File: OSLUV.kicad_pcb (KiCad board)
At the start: 4 copper layers, 110 x 50 mm, 72 parts, among them IC1 NCP12510ASN65T1G, IC2 SFH6156-3, Q1 STD3NK80ZT4, Q2 BAT847B, T1 750343466, U2 TL432DBZ

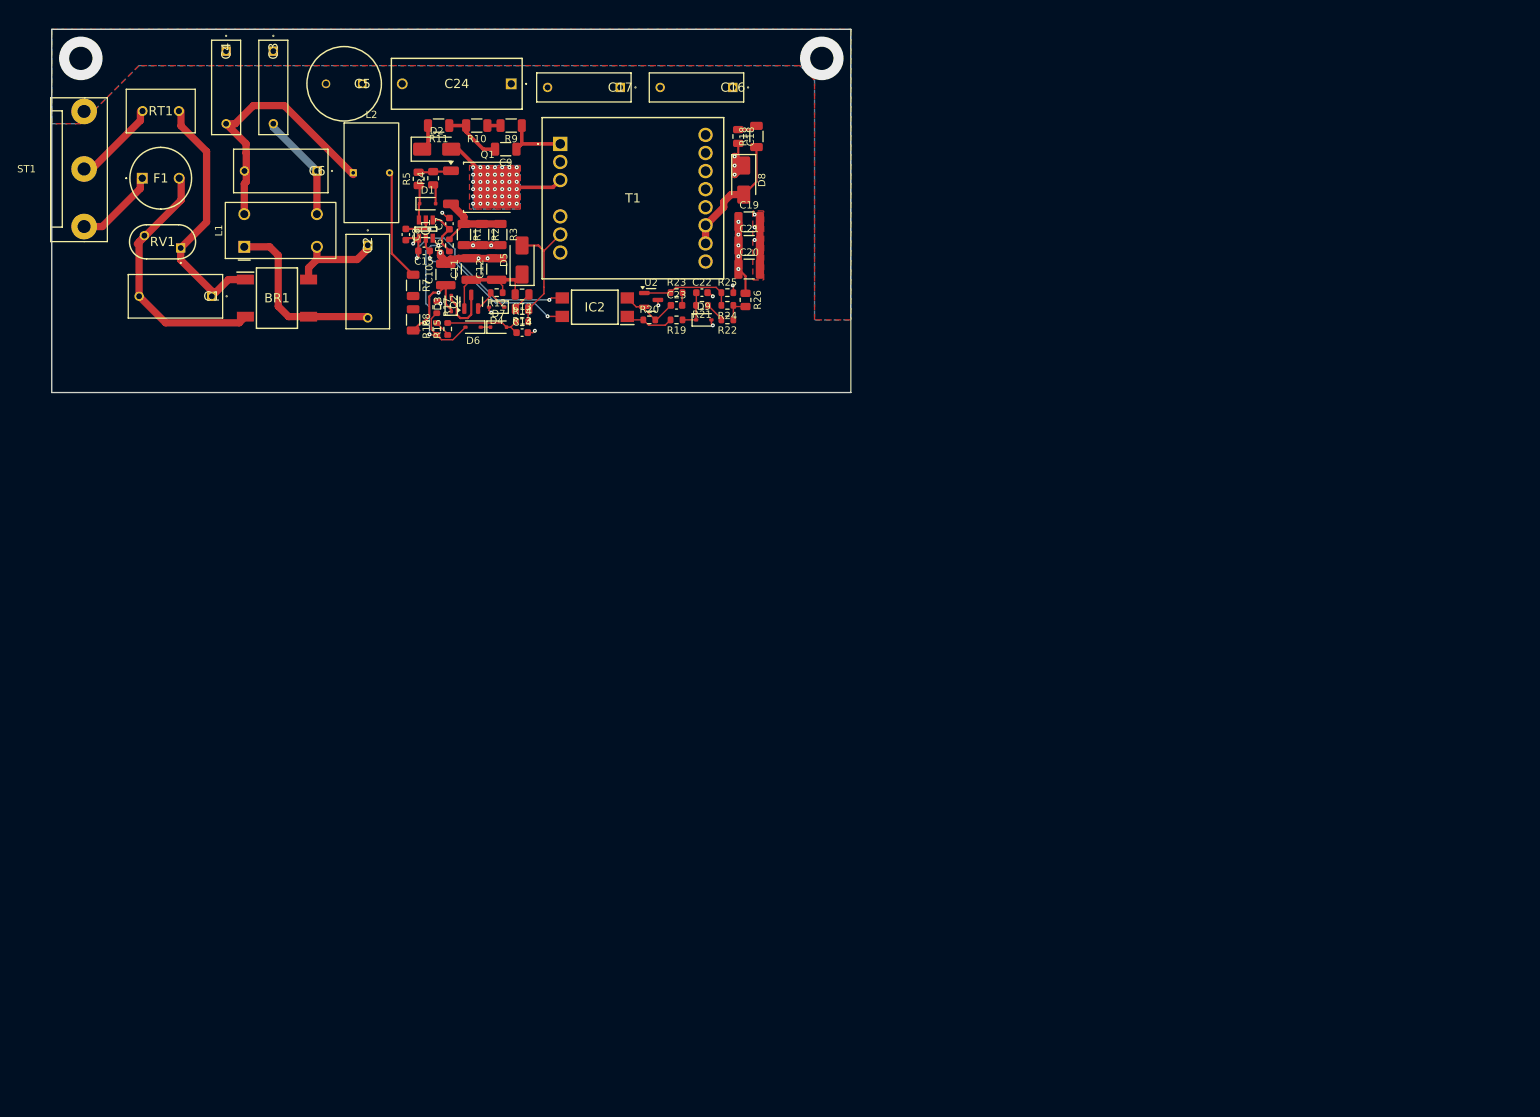
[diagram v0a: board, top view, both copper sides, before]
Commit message: update of schematic
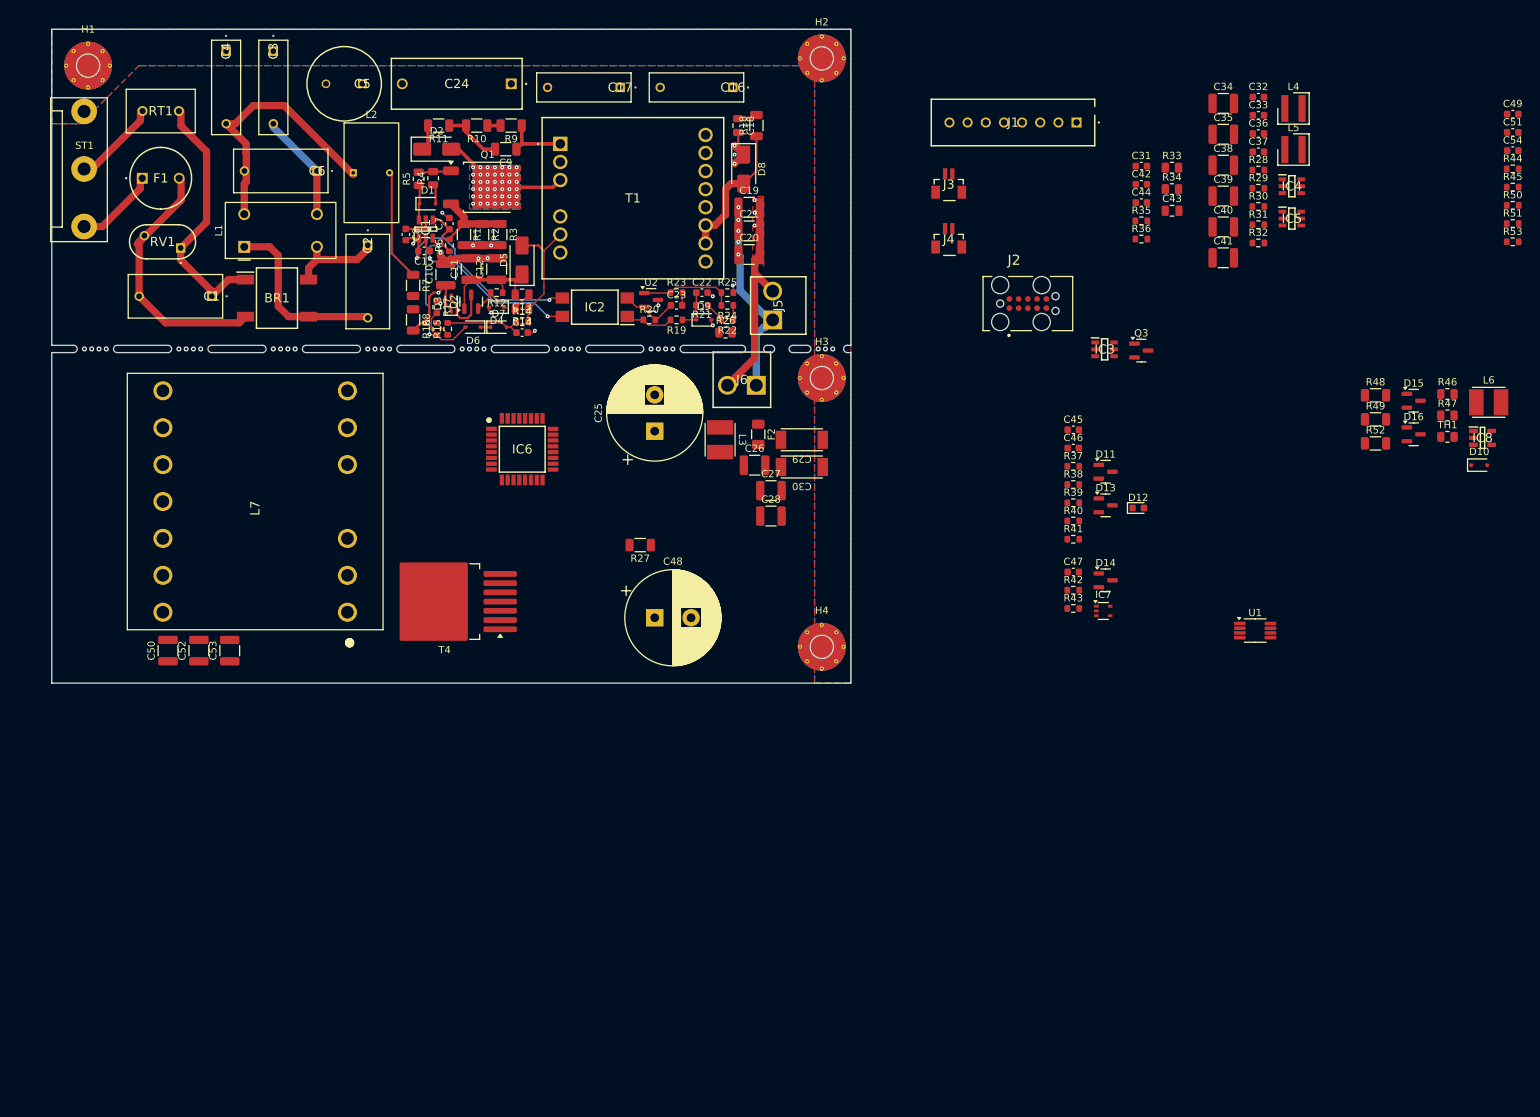
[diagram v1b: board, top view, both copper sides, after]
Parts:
- added C25: 330µ 35V, Capacitor_THT:CP_Radial_D13.0mm_P5.00mm, F.Cu at (133.0, 105.3)
- added C26: 10µ X7R 50V 1210, Capacitor_SMD:C_1210_3225Metric, F.Cu at (146.8, 110.0)
- added C27: 10µ X7R 50V 1210, Capacitor_SMD:C_1210_3225Metric, F.Cu at (149.0, 113.5)
- added C28: 10µ X7R 50V 1210, Capacitor_SMD:C_1210_3225Metric, F.Cu at (149.0, 117.0)
- added C29: 2211_8853522130151, Capacitor_SMD_Wurth:C_Wurth_WCAP-CSSA-2211, F.Cu at (153.2, 106.5)
- added C30: 2211_8853522130151, Capacitor_SMD_Wurth:C_Wurth_WCAP-CSSA-2211, F.Cu at (153.2, 110.2)
- added C31: 100n 0603, Capacitor_SMD:C_0603_1608Metric, F.Cu at (200.0, 68.8)
- added C32: 100n 50V 0603, Capacitor_SMD:C_0603_1608Metric, F.Cu at (216.1, 59.3)
- added C33: 100n 50V 0603, Capacitor_SMD:C_0603_1608Metric, F.Cu at (216.1, 61.8)
- added C34: 10u X7R 1210, Capacitor_SMD:C_1210_3225Metric, F.Cu at (211.3, 60.2)
- added C35: 10u X7R 1210, Capacitor_SMD:C_1210_3225Metric, F.Cu at (211.3, 64.5)
- added C36: 100n 50V 0603, Capacitor_SMD:C_0603_1608Metric, F.Cu at (216.1, 64.3)
- added C37: 100n 50V 0603, Capacitor_SMD:C_0603_1608Metric, F.Cu at (216.1, 66.9)
- added C38: 10u X7R 1210, Capacitor_SMD:C_1210_3225Metric, F.Cu at (211.3, 68.7)
- added C39: 10u X7R 1210, Capacitor_SMD:C_1210_3225Metric, F.Cu at (211.3, 73.0)
- added C40: 10u X7R 1210, Capacitor_SMD:C_1210_3225Metric, F.Cu at (211.3, 77.2)
- added C41: 10u X7R 1210, Capacitor_SMD:C_1210_3225Metric, F.Cu at (211.3, 81.5)
- added C42: 100n 0603, Capacitor_SMD:C_0603_1608Metric, F.Cu at (200.0, 71.3)
- added C43: 1u X7R 50V 0805, Capacitor_SMD:C_0805_2012Metric, F.Cu at (204.2, 75.0)
- added C44: 100n 0603, Capacitor_SMD:C_0603_1608Metric, F.Cu at (200.0, 73.8)
- added C45: 1n 0603, Capacitor_SMD:C_0603_1608Metric, F.Cu at (190.6, 105.1)
- added C46: 100n 0603, Capacitor_SMD:C_0603_1608Metric, F.Cu at (190.6, 107.6)
- added C47: 100n 0603, Capacitor_SMD:C_0603_1608Metric, F.Cu at (190.6, 124.7)
- added C48: 330u 35V, Capacitor_THT:CP_Radial_D13.0mm_P5.00mm, F.Cu at (133.0, 131.0)
- added C49: 100p 0603, Capacitor_SMD:C_0603_1608Metric, F.Cu at (251.1, 61.7)
- added C50: 10µ X7R 50V 1210, Capacitor_SMD:C_1210_3225Metric, F.Cu at (66.0, 135.5)
- added C51: 100p 0603, Capacitor_SMD:C_0603_1608Metric, F.Cu at (251.1, 64.2)
- added C52: 10µ X7R 50V 1210, Capacitor_SMD:C_1210_3225Metric, F.Cu at (70.2, 135.5)
- added C53: 10µ X7R 50V 1210, Capacitor_SMD:C_1210_3225Metric, F.Cu at (74.5, 135.5)
- added C54: 100p 0603, Capacitor_SMD:C_0603_1608Metric, F.Cu at (251.1, 66.7)
- added D10: BAT54J, Diode_SMD:D_SOD-323F, F.Cu at (246.5, 110.0)
- added D11: BAS40-04, Package_TO_SOT_SMD:SOT-23, F.Cu at (195.1, 110.9)
- added D12: LED gr 0603, LED_SMD:LED_0603_1608Metric, F.Cu at (199.6, 115.9)
- added D13: BAS40-04, Package_TO_SOT_SMD:SOT-23, F.Cu at (195.1, 115.5)
- added D14: BAS40-04, Package_TO_SOT_SMD:SOT-23, F.Cu at (195.1, 125.8)
- added D15: BAS40-04, Package_TO_SOT_SMD:SOT-23, F.Cu at (237.5, 101.1)
- added D16: BAS40-04, Package_TO_SOT_SMD:SOT-23, F.Cu at (237.5, 105.8)
- added F2: 2A, Fuse:Fuse_1206_3216Metric, F.Cu at (147.2, 105.8)
- added H1: MountingHole_Pad, Hansmann:Mounting_M3_NPTH_Vias, F.Cu at (55.0, 55.0)
- added H2: MountingHole_Pad, Hansmann:Mounting_M3_NPTH_Vias, F.Cu at (156.0, 54.0)
- added H3: MountingHole_Pad, Hansmann:Mounting_M3_NPTH_Vias, F.Cu at (156.0, 98.0)
- added H4: MountingHole_Pad, Hansmann:Mounting_M3_NPTH_Vias, F.Cu at (156.0, 135.0)
- added IC3: INA210, Hansmann:SOT95P280X90-6N, F.Cu at (194.9, 94.0)
- added IC4: AP63300WU-7, Hansmann:SOT95P280X90-6N, F.Cu at (220.7, 71.6)
- added IC5: AP63300WU-7, Hansmann:SOT95P280X90-6N, F.Cu at (220.7, 76.0)
- added IC6: STM32G071KBT6, Hansmann:QFP80P900X900X160-32N, F.Cu at (114.8, 107.8)
- added IC7: TLV9001IDBVR, Package_TO_SOT_SMD:SOT-353_SC-70-5, F.Cu at (194.7, 130.1)
- added IC8: FAN3100TSX, Hansmann:SOT95P280X145-5N, F.Cu at (247.0, 106.2)
- added J1: B08B-XASK-1-A_LF__SN_, Hansmann:B08BXASK1ALFSN, F.Cu at (191.1, 62.8)
- added J2: TC2050-IDC, Hansmann:TAG-CONNECT_TC2050-IDC, F.Cu at (184.4, 87.8)
- added J3: BM02B-SRSS-TB_LF__SN_, Hansmann:BM02BSRSSTBLFSN, F.Cu at (173.5, 71.7)
- added J4: BM02B-SRSS-TB_LF__SN_, Hansmann:BM02BSRSSTBLFSN, F.Cu at (173.5, 79.3)
- added J5: 640445-2, Hansmann:6404452, F.Cu at (149.2, 90.0)
- added J6: 640445-2, Hansmann:6404452, F.Cu at (147.0, 99.0)
- added L3: 1812_744045008, Inductor_SMD_Wurth:L_Wurth_WE-LQ-1812, F.Cu at (142.0, 106.5)
- added L4: 4030_74438357068, Inductor_SMD_Wurth:L_Wurth_WE-MAPI-4030, F.Cu at (220.9, 60.9)
- added L5: 4030_74438357068, Inductor_SMD_Wurth:L_Wurth_WE-MAPI-4030, F.Cu at (220.9, 66.5)
- added L6: 1812_744045008, Inductor_SMD_Wurth:L_Wurth_WE-LQ-1812, F.Cu at (247.8, 101.3)
- added L7: ETD29, Hansmann:B66359B1013T001, F.Cu at (78.0, 115.0)
- added Q3: BSS138, Package_TO_SOT_SMD:SOT-23, F.Cu at (200.0, 94.2)
- added R27: 0R02 1% 1206, Resistor_SMD:R_1206_3216Metric, F.Cu at (131.0, 121.0)
- added R28: 12k 0603, Resistor_SMD:R_0603_1608Metric, F.Cu at (216.1, 69.4)
- added R29: 1Meg 0603, Resistor_SMD:R_0603_1608Metric, F.Cu at (216.1, 71.9)
- added R30: 39k 0603, Resistor_SMD:R_0603_1608Metric, F.Cu at (216.1, 74.4)
- added R31: 10k 0603, Resistor_SMD:R_0603_1608Metric, F.Cu at (216.1, 76.9)
- added R32: 180k 0603, Resistor_SMD:R_0603_1608Metric, F.Cu at (216.1, 79.4)
- added R33: 180R 0805, Resistor_SMD:R_0805_2012Metric, F.Cu at (204.2, 69.0)
- added R34: 180R 0805, Resistor_SMD:R_0805_2012Metric, F.Cu at (204.2, 72.0)
- added R35: 10R 0603, Resistor_SMD:R_0603_1608Metric, F.Cu at (200.0, 76.4)
- added R36: 10k 0603, Resistor_SMD:R_0603_1608Metric, F.Cu at (200.0, 78.9)
- added R37: 10k 0603, Resistor_SMD:R_0603_1608Metric, F.Cu at (190.6, 110.2)
- added R38: 1k5 0603, Resistor_SMD:R_0603_1608Metric, F.Cu at (190.6, 112.7)
- added R39: 10k 0603, Resistor_SMD:R_0603_1608Metric, F.Cu at (190.6, 115.2)
- added R40: 1k 0603, Resistor_SMD:R_0603_1608Metric, F.Cu at (190.6, 117.7)
- added R41: 10k 0603, Resistor_SMD:R_0603_1608Metric, F.Cu at (190.6, 120.2)
- added R42: 1k 0603, Resistor_SMD:R_0603_1608Metric, F.Cu at (190.6, 127.2)
- added R43: 4k7 0603, Resistor_SMD:R_0603_1608Metric, F.Cu at (190.6, 129.7)
- added R44: 100R 0603, Resistor_SMD:R_0603_1608Metric, F.Cu at (251.1, 69.2)
- added R45: 10k 0603, Resistor_SMD:R_0603_1608Metric, F.Cu at (251.1, 71.7)
- added R46: 3R3 0805, Resistor_SMD:R_0805_2012Metric, F.Cu at (242.1, 100.2)
- added R47: 33R 0805, Resistor_SMD:R_0805_2012Metric, F.Cu at (242.1, 103.2)
- added R48: 1R 1206, Resistor_SMD:R_1206_3216Metric, F.Cu at (232.2, 100.4)
- added R49: 1R 1206, Resistor_SMD:R_1206_3216Metric, F.Cu at (232.2, 103.7)
- added R50: 1k 0603, Resistor_SMD:R_0603_1608Metric, F.Cu at (251.1, 74.2)
- added R51: 10k 0603, Resistor_SMD:R_0603_1608Metric, F.Cu at (251.1, 76.7)
- added R52: 1R 1206, Resistor_SMD:R_1206_3216Metric, F.Cu at (232.2, 107.0)
- added R53: 1k 0603, Resistor_SMD:R_0603_1608Metric, F.Cu at (251.1, 79.2)
- added T4: NMOS_GDS-KS_SMD, Hansmann:TO-263-7_TabPin2, F.Cu at (104.1, 128.8)
- added TH1: NTC xxx, Resistor_SMD:R_0805_2012Metric, F.Cu at (242.1, 106.1)
- added U1: OPA2356AIDGKR, Package_SO:VSSOP-8_3x3mm_P0.65mm, F.Cu at (215.7, 132.8)
- moved R26 5.27 mm to (142.8, 91.8), turned to 0 degrees
- moved C19 2.00 mm to (146.0, 74.5)
- moved C20 2.00 mm to (146.0, 81.0)
- moved C21 2.00 mm to (146.0, 77.8)
- moved C18 1.50 mm to (144.5, 63.2)
- moved D8 1.50 mm to (145.2, 69.2)
- moved R18 1.50 mm to (147.0, 63.2)
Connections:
- net /offlineConverter/24V_out renamed /excimerDriver/VDC
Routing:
- net GND: track 10.1 -> 65.4 mm
- net /excimerDriver/VDC: track 26.4 -> 65.7 mm
- net Net-(D8-A): track 17.2 -> 19.4 mm
- net Net-(R22-Pad1): track 3.74 -> 2.23 mm
- net Earth: vias 2 -> 3
- net (no net): vias 0 -> 28
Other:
- board size 110 x 50 mm -> 110 x 90 mm

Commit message: schematic done, not placed
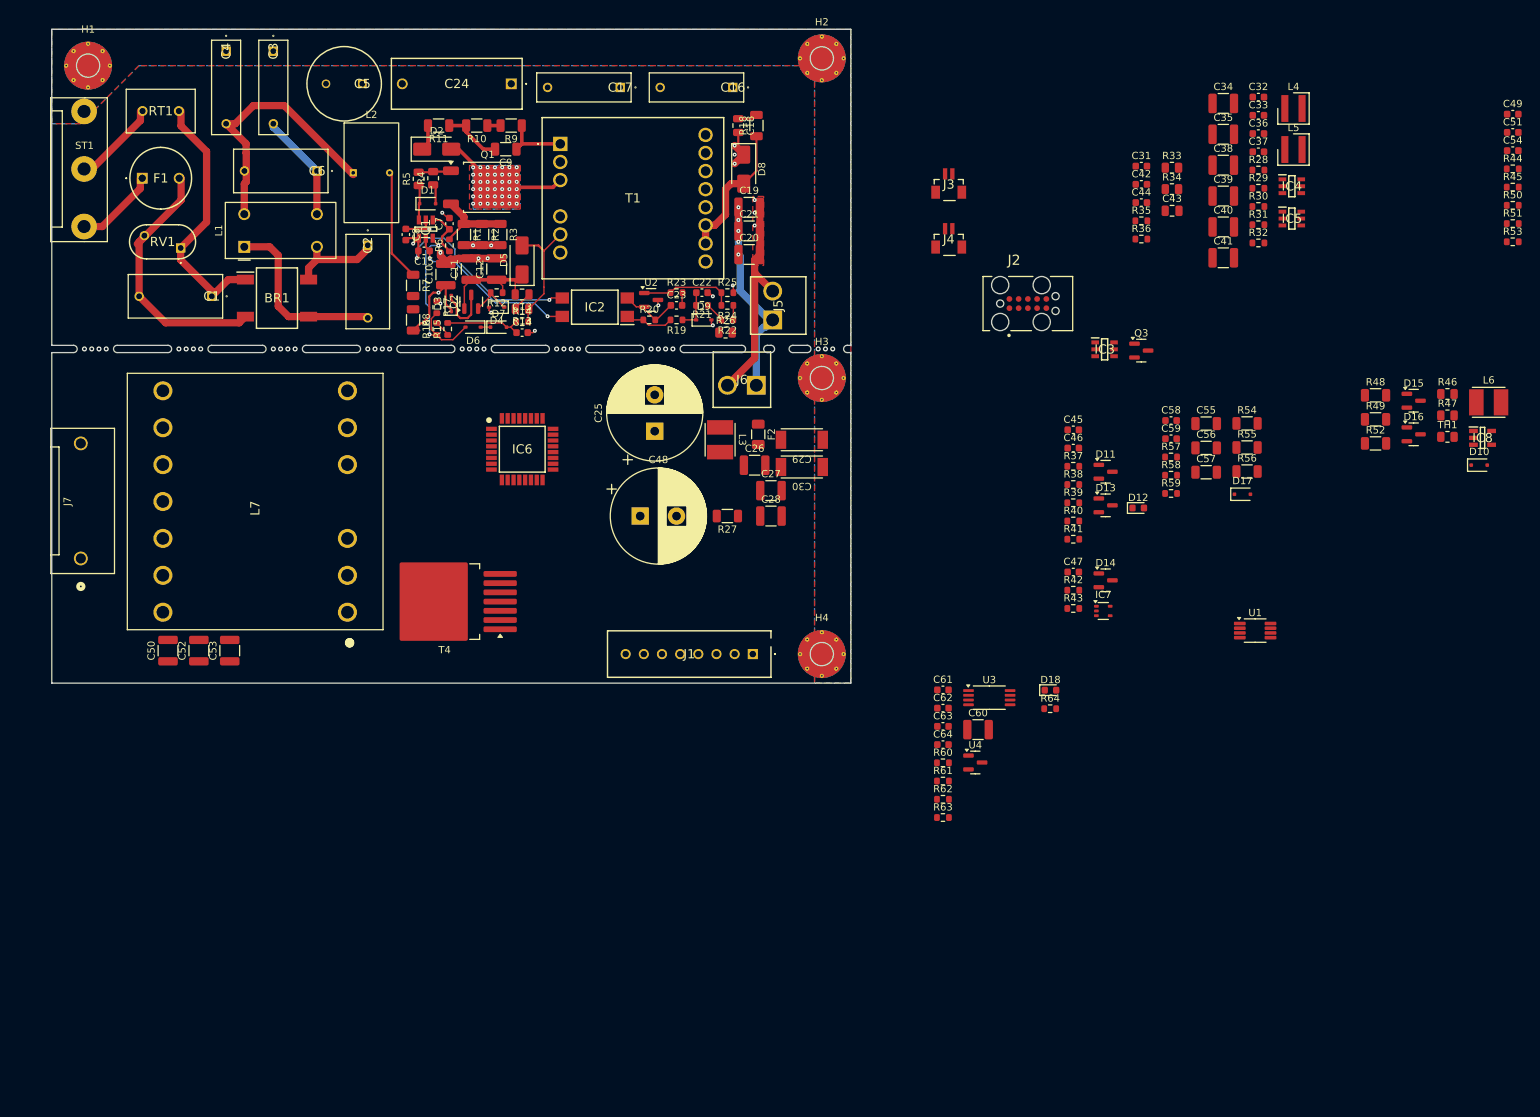
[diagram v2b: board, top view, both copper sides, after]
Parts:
- added C55: 10p 1% 600V 1206, Capacitor_SMD:C_1206_3216Metric, F.Cu at (208.9, 104.3)
- added C56: 10p 1% 600V 1206, Capacitor_SMD:C_1206_3216Metric, F.Cu at (208.9, 107.6)
- added C57: 10p 1% 600V 1206, Capacitor_SMD:C_1206_3216Metric, F.Cu at (208.9, 111.0)
- added C58: 1n8 1% C0G 0603, Capacitor_SMD:C_0603_1608Metric, F.Cu at (204.1, 103.8)
- added C59: 1n 0603, Capacitor_SMD:C_0603_1608Metric, F.Cu at (204.1, 106.4)
- added C60: 10µ X7R 50V 1210, Capacitor_SMD:C_1210_3225Metric, F.Cu at (177.5, 146.4)
- added C61: 100n 0603, Capacitor_SMD:C_0603_1608Metric, F.Cu at (172.7, 140.9)
- added C62: 100n 0603, Capacitor_SMD:C_0603_1608Metric, F.Cu at (172.7, 143.4)
- added C63: 100p 0603, Capacitor_SMD:C_0603_1608Metric, F.Cu at (172.7, 145.9)
- added C64: 100p 0603, Capacitor_SMD:C_0603_1608Metric, F.Cu at (172.7, 148.5)
- added D17: BAT54J, Diode_SMD:D_SOD-323F, F.Cu at (213.9, 114.0)
- added D18: LED gr 0603, LED_SMD:LED_0603_1608Metric, F.Cu at (187.5, 141.0)
- added J7: B5P-VH, Hansmann:CONN_B2P5-VH_JST, F.Cu at (54.0, 122.8)
- added R54: 1Meg 0.1% 500V 1206, Resistor_SMD:R_1206_3216Metric, F.Cu at (214.5, 104.2)
- added R55: 1Meg 0.1% 500V 1206, Resistor_SMD:R_1206_3216Metric, F.Cu at (214.5, 107.6)
- added R56: 1Meg 0.1% 500V 1206, Resistor_SMD:R_1206_3216Metric, F.Cu at (214.5, 110.9)
- added R57: 5k6 0.1% 0603, Resistor_SMD:R_0603_1608Metric, F.Cu at (204.1, 108.9)
- added R58: 33R 0603, Resistor_SMD:R_0603_1608Metric, F.Cu at (204.1, 111.4)
- added R59: 10Meg 0603, Resistor_SMD:R_0603_1608Metric, F.Cu at (204.1, 113.9)
- added R60: 10k 0603, Resistor_SMD:R_0603_1608Metric, F.Cu at (172.7, 151.0)
- added R61: 10k 0603, Resistor_SMD:R_0603_1608Metric, F.Cu at (172.7, 153.5)
- added R62: 10k 0603, Resistor_SMD:R_0603_1608Metric, F.Cu at (172.7, 156.0)
- added R63: 1k 0603, Resistor_SMD:R_0603_1608Metric, F.Cu at (172.7, 158.5)
- added R64: 1k5 0603, Resistor_SMD:R_0603_1608Metric, F.Cu at (187.4, 143.5)
- added U3: LM2903, Package_SO:TSSOP-8_4.4x3mm_P0.65mm, F.Cu at (179.1, 142.0)
- added U4: AZ431LANTR, Package_TO_SOT_SMD:SOT-23, F.Cu at (177.1, 150.9)
- U2: value TL432DBZ -> AZ431LANTR
- moved J1 85.7 mm to (146.5, 136.0)
- moved C48 14.1 mm to (131.0, 117.0)
- moved R27 12.6 mm to (143.0, 117.0)
- moved H4 1.00 mm to (156.0, 136.0)
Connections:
- net /excimerDriver/Lamp_GND renamed /excimerDriver/lampDriver/Lamp_GND
- net Net-(C50-Pad1) renamed /excimerDriver/lampDriver/VDC_Trafo
- net Net-(IC6-PB9) renamed /excimerDriver/MCU_REMOTE
- D16 pad 3: Net-(U1A-+) -> Net-(D16-Pad3)
- IC6 pad 10: unconnected-(IC6-PA3-Pad10) -> /excimerDriver/Usense_Lamp
- IC6 pad 11: unconnected-(IC6-PA4-Pad11) -> /excimerDriver/Ilevel_DAC
- IC6 pad 13: unconnected-(IC6-PA6-Pad13) -> /excimerDriver/OCP
- IC6 pad 14: unconnected-(IC6-PA7-Pad14) -> /excimerDriver/Status
- IC6 pad 22: unconnected-(IC6-PA11_[PA9]-Pad22) -> /excimerDriver/PeakCurrent
- IC6 pad 24: unconnected-(IC6-PA13-Pad24) -> /excimerDriver/SWDIO
- IC6 pad 25: unconnected-(IC6-PA14-BOOT0-Pad25) -> /excimerDriver/SWCLK
- IC6 pad 26: unconnected-(IC6-PD0-Pad26) -> /excimerDriver/CMD_RX
- IC6 pad 3: unconnected-(IC6-PC15-OSC32_OUT-Pad3) -> Net-(IC6-PC15-OSC32_OUT)
- IC6 pad 8: unconnected-(IC6-PA1-Pad8) -> /excimerDriver/temp_MOSFET
- IC6 pad 9: unconnected-(IC6-PA2-Pad9) -> /excimerDriver/CMD_TX
- L7 pad 8: /excimerDriver/Lamp_HV -> /excimerDriver/lampDriver/Lamp_HV
- R44 pad 1: /excimerDriver/lampDriver/DRV -> /excimerDriver/DRV
- R51 pad 2: /excimerDriver/lampDriver/temp_MOSFET -> /excimerDriver/temp_MOSFET
- R53 pad 1: Net-(U1A-+) -> Net-(D16-Pad3)
- TH1 pad 1: /excimerDriver/lampDriver/temp_MOSFET -> /excimerDriver/temp_MOSFET
- U1 pad 1: +3V3 -> /excimerDriver/Usense_Lamp
- U1 pad 2: +3V3 -> /excimerDriver/Usense_Lamp
- U1 pad 5: unconnected-(U1B-+-Pad5) -> Net-(U1B-+)
- U1 pad 6: unconnected-(U1B---Pad6) -> Net-(D17-K)
- U1 pad 7: unconnected-(U1-Pad7) -> Net-(D17-A)

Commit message: restore to 9.0
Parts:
- moved L6 169.8 mm to (82.0, 138.0)
- moved D15 138.3 mm to (105.9, 143.8)
- moved D16 138.3 mm to (105.9, 148.4)
- moved R48 138.3 mm to (100.7, 143.0)
- moved R49 138.3 mm to (100.7, 146.3)
- moved R52 138.3 mm to (100.7, 149.7)
- moved TH1 138.3 mm to (110.6, 148.8)
- moved R46 128.9 mm to (117.0, 131.0), turned to 180 degrees
- moved D10 128.6 mm to (119.8, 132.0), turned to 90 degrees
- moved R47 128.6 mm to (117.0, 133.0), turned to 180 degrees
- moved IC8 126.6 mm to (123.0, 132.0), turned to 180 degrees
- moved C36 118.1 mm to (135.4, 150.6)
- moved R29 118.1 mm to (135.4, 158.1)
- moved R32 118.1 mm to (135.4, 165.6)
- moved C32 118.1 mm to (135.4, 145.5)
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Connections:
- IC8 pad 5: Net-(IC8-OUT) -> Net-(D10-K)
- R46 pad 1: Net-(IC8-OUT) -> Net-(D10-A)
- R46 pad 2: Net-(D10-K) -> Net-(T4-G)
- R47 pad 1: Net-(IC8-OUT) -> Net-(D10-K)
- R47 pad 2: Net-(D10-A) -> Net-(T4-G)
- T4 pad 1: Net-(D10-A) -> Net-(T4-G)
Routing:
- net GND: track 65.4 -> 117.2 mm
- net /excimerDriver/VDC: track 65.7 -> 102.9 mm
- net Net-(T4-G): track 0.00 -> 7.36 mm
- net Net-(D10-K): track 0.00 -> 3.94 mm
- net Net-(D10-A): track 0.00 -> 1.88 mm
